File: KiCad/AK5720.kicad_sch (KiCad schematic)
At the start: 20 parts, among them J6 AudioJack3_Dual_Switch, U4 AK5720VT

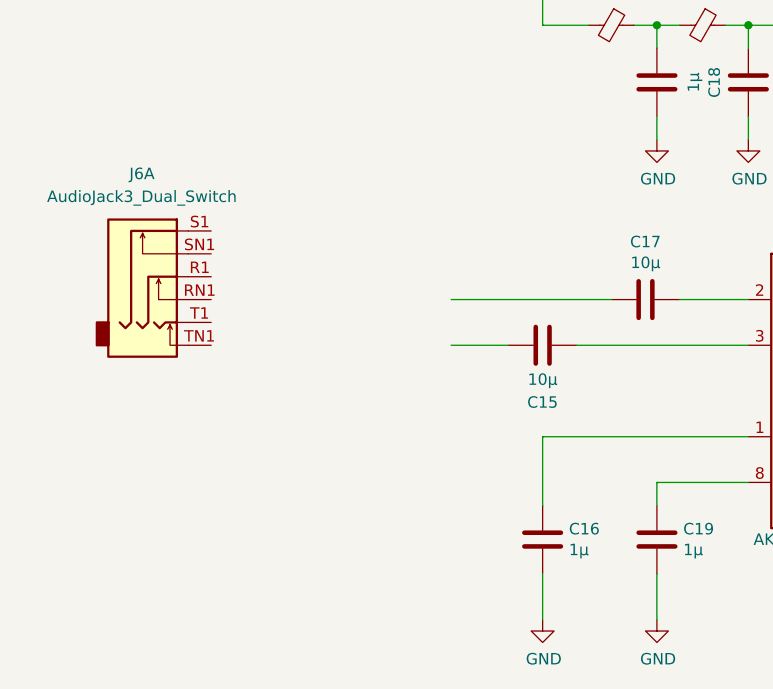
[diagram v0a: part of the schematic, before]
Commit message: -associated footprints to more specific components -added manufacturer and part series info to more specific components
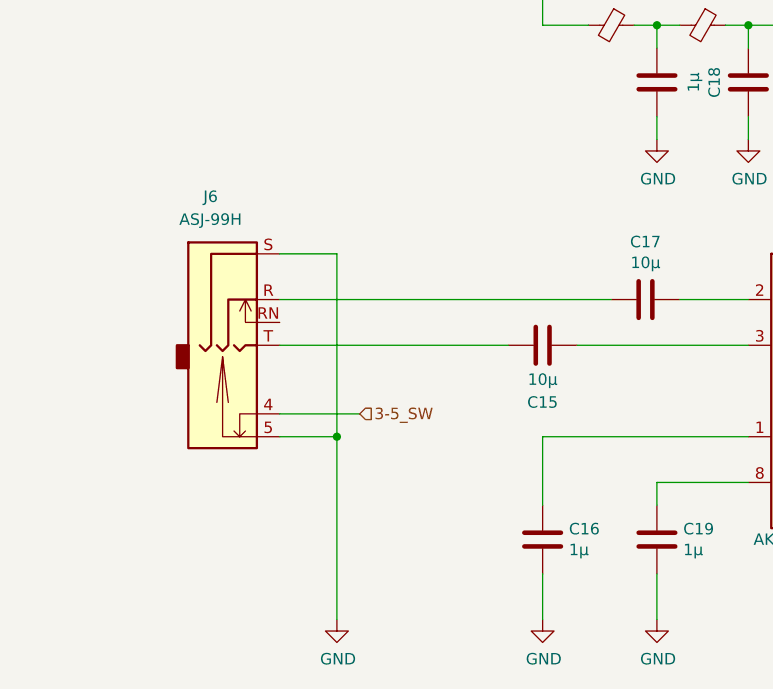
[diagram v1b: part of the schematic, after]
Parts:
- J6: value AudioJack3_Dual_Switch -> ASJ-99H; footprint (none) -> custom_footprints:ASJ-99H; symbol Connector:AudioJack3_Dual_Switch -> custom_symbols:AudioJack_ASJ-99H; MFG (none) -> Adam Tech; MFG# (none) -> ASJ-99H-R-HT-T/R
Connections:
- net GND: now also J6.5, J6.S
- net at C15.2: now also J6.T
- net at C17.2: now also J6.R
- new net 3-5_SW: J6.4
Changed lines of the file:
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@@
   (junction (at 142.24 68.58) (diameter 0) (color 0 0 0 0)
   )
+  (junction (at 81.28 114.3) (diameter 0) (color 0 0 0 0)
+  )
   (junction (at 198.12 114.3) (diameter 0) (color 0 0 0 0)
   )
@@
     (stroke (width 0) (type default) (color 0 0 0 0))
   )
-  (wire (pts (xy 100.33 104.14) (xy 93.98 104.14))
+  (wire (pts (xy 74.93 104.14) (xy 100.33 104.14))
     (stroke (width 0) (type default) (color 0 0 0 0))
   )
@@
     (stroke (width 0) (type default) (color 0 0 0 0))
   )
+  (wire (pts (xy 81.28 93.98) (xy 81.28 114.3))
+    (stroke (width 0) (type default) (color 0 0 0 0))
+  )
   (wire (pts (xy 190.5 134.62) (xy 190.5 132.08))
     (stroke (width 0) (type default) (color 0 0 0 0))
@@
     (stroke (width 0) (type default) (color 0 0 0 0))
   )
+  (wire (pts (xy 74.93 111.76) (xy 83.82 111.76))
+    (stroke (width 0) (type default) (color 0 0 0 0))
+  )
   (wire (pts (xy 152.4 121.92) (xy 182.88 121.92))
     (stroke (width 0) (type default) (color 0 0 0 0))
@@
     (stroke (width 0) (type default) (color 0 0 0 0))
   )
+  (wire (pts (xy 81.28 114.3) (xy 81.28 134.62))
+    (stroke (width 0) (type default) (color 0 0 0 0))
+  )
+  (wire (pts (xy 74.93 114.3) (xy 81.28 114.3))
+    (stroke (width 0) (type default) (color 0 0 0 0))
+  )
   (wire (pts (xy 114.3 68.58) (xy 116.84 68.58))
     (stroke (width 0) (type default) (color 0 0 0 0))
@@
     (stroke (width 0) (type default) (color 0 0 0 0))
   )
-  (wire (pts (xy 111.76 99.06) (xy 93.98 99.06))
+  (wire (pts (xy 74.93 99.06) (xy 111.76 99.06))
     (stroke (width 0) (type default) (color 0 0 0 0))
   )
@@
     (stroke (width 0) (type default) (color 0 0 0 0))
   )
+  (wire (pts (xy 74.93 93.98) (xy 81.28 93.98))
+    (stroke (width 0) (type default) (color 0 0 0 0))
+  )
   (wire (pts (xy 116.84 81.28) (xy 116.84 78.74))
     (stroke (width 0) (type default) (color 0 0 0 0))
@@
   )
   (hierarchical_label "SDWS" (shape output) (at 165.1 101.6 0)
+    (effects (font (size 1.27 1.27)) (justify left))
+  )
+  (hierarchical_label "3-5_SW" (shape input) (at 83.82 111.76 0)
     (effects (font (size 1.27 1.27)) (justify left))
   )
@@
     (pin "2")
   )
-  (symbol (lib_id "Connector:AudioJack3_Dual_Switch") (at 62.23 96.52 0) (unit 1)
+  (symbol (lib_id "custom_symbols:AudioJack_ASJ-99H") (at 69.85 99.06 0) (unit 1)
     (in_bom yes) (on_board yes) (fields_autoplaced)
-    (property "Reference" "J6" (id 0) (at 59.6265 85.09 0))
-    (property "Value" "AudioJack3_Dual_Switch" (id 1) (at 59.6265 87.63 0))
-    (property "Footprint" "" (id 2) (at 60.96 96.52 0)
-      (effects (font (size 1.27 1.27)) hide)
-    )
-    (property "Datasheet" "~" (id 3) (at 60.96 96.52 0)
-      (effects (font (size 1.27 1.27)) hide)
-    )
-    (pin "R1")
-    (pin "RN1")
-    (pin "S1")
-    (pin "SN1")
-    (pin "T1")
-    (pin "TN1")
-    (pin "R2")
-    (pin "RN2")
-    (pin "S2")
-    (pin "SN2")
-    (pin "T2")
-    (pin "TN2")
+    (property "Reference" "J6" (id 0) (at 67.2465 87.63 0))
+    (property "Value" "ASJ-99H" (id 1) (at 67.2465 90.17 0))
+    (property "Footprint" "custom_footprints:ASJ-99H" (id 2) (at 69.85 99.06 0)
+      (effects (font (size 1.27 1.27)) hide)
+    )
+    (property "Datasheet" "~" (id 3) (at 69.85 99.06 0)
+      (effects (font (size 1.27 1.27)) hide)
+    )
+    (property "MFG" "Adam Tech" (id 4) (at 69.85 99.06 0)
+      (effects (font (size 1.27 1.27)) hide)
+    )
+    (property "MFG#" "ASJ-99H-R-HT-T/R" (id 5) (at 69.85 99.06 0)
+      (effects (font (size 1.27 1.27)) hide)
+    )
+    (pin "4")
+    (pin "5")
+    (pin "R")
+    (pin "RN")
+    (pin "S")
+    (pin "T")
+  )
+  (symbol (lib_id "power:GND") (at 81.28 134.62 0) (unit 1)
+    (in_bom yes) (on_board yes)
+    (property "Reference" "#PWR?" (id 0) (at 81.28 140.97 0)
+      (effects (font (size 1.27 1.27)) hide)
+    )
+    (property "Value" "GND" (id 1) (at 81.407 139.0142 0))
+    (property "Footprint" "" (id 2) (at 81.28 134.62 0)
+      (effects (font (size 1.27 1.27)) hide)
+    )
+    (property "Datasheet" "" (id 3) (at 81.28 134.62 0)
+      (effects (font (size 1.27 1.27)) hide)
+    )
+    (pin "1")
   )
   (symbol (lib_id "power:+3V3") (at 142.24 64.77 0) (unit 1)

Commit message: -boards on hand atm, assembling first board and finalizing used component values
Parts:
- C15, C17: value 10µ -> 1u
- C16, C18, C19, C21: value 1µ -> 1u
- C20: value 220n -> 1u
- R32: value R -> 22R
- R33, R35, R38, R40: value R -> 0R
- R34, R36, R37, R39: value R -> NP
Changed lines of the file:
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@@
       (effects (font (size 1.27 1.27)) (justify left))
     )
-    (property "Value" "R" (id 1) (at 207.518 129.413 0)
+    (property "Value" "0R" (id 1) (at 207.518 129.413 0)
       (effects (font (size 1.27 1.27)) (justify left))
     )
@@
     (in_bom yes) (on_board yes)
     (property "Reference" "C15" (id 0) (at 104.14 110.49 90))
-    (property "Value" "10µ" (id 1) (at 104.14 107.95 90))
+    (property "Value" "1u" (id 1) (at 104.14 107.95 90))
     (property "Footprint" "Capacitor_SMD:C_0603_1608Metric" (id 2) (at 100.33 105.1052 0)
       (effects (font (size 1.27 1.27)) hide)
@@
       (effects (font (size 1.27 1.27)) (justify left))
     )
-    (property "Value" "R" (id 1) (at 199.898 129.413 0)
+    (property "Value" "0R" (id 1) (at 199.898 129.413 0)
       (effects (font (size 1.27 1.27)) (justify left))
     )
@@
       (effects (font (size 1.27 1.27)) (justify left))
     )
-    (property "Value" "R" (id 1) (at 199.898 104.013 0)
+    (property "Value" "NP" (id 1) (at 199.898 104.013 0)
       (effects (font (size 1.27 1.27)) (justify left))
     )
@@
     (in_bom yes) (on_board yes)
     (property "Reference" "C18" (id 0) (at 123.2408 74.93 90))
-    (property "Value" "1µ" (id 1) (at 120.9294 74.93 90))
+    (property "Value" "1u" (id 1) (at 120.9294 74.93 90))
     (property "Footprint" "Capacitor_SMD:C_0603_1608Metric" (id 2) (at 115.8748 71.12 0)
       (effects (font (size 1.27 1.27)) hide)
@@
       (effects (font (size 1.27 1.27)) (justify left))
     )
-    (property "Value" "R" (id 1) (at 159.893 94.742 0)
+    (property "Value" "22R" (id 1) (at 159.893 94.742 0)
       (effects (font (size 1.27 1.27)) (justify left))
     )
@@
       (effects (font (size 1.27 1.27)) (justify left))
     )
-    (property "Value" "1µ" (id 1) (at 119.761 126.873 0)
+    (property "Value" "1u" (id 1) (at 119.761 126.873 0)
       (effects (font (size 1.27 1.27)) (justify left))
     )
@@
     (in_bom yes) (on_board yes)
     (property "Reference" "C21" (id 0) (at 153.7208 74.93 90))
-    (property "Value" "1µ" (id 1) (at 151.4094 74.93 90))
+    (property "Value" "1u" (id 1) (at 151.4094 74.93 90))
     (property "Footprint" "Capacitor_SMD:C_0603_1608Metric" (id 2) (at 146.3548 71.12 0)
       (effects (font (size 1.27 1.27)) hide)
@@
       (effects (font (size 1.27 1.27)) (justify left))
     )
-    (property "Value" "R" (id 1) (at 207.518 104.013 0)
+    (property "Value" "NP" (id 1) (at 207.518 104.013 0)
       (effects (font (size 1.27 1.27)) (justify left))
     )
@@
       (effects (font (size 1.27 1.27)) (justify left))
     )
-    (property "Value" "R" (id 1) (at 184.658 104.013 0)
+    (property "Value" "0R" (id 1) (at 184.658 104.013 0)
       (effects (font (size 1.27 1.27)) (justify left))
     )
@@
       (effects (font (size 1.27 1.27)) (justify left))
     )
-    (property "Value" "R" (id 1) (at 192.278 129.413 0)
+    (property "Value" "NP" (id 1) (at 192.278 129.413 0)
       (effects (font (size 1.27 1.27)) (justify left))
     )
@@
       (effects (font (size 1.27 1.27)) (justify left))
     )
-    (property "Value" "R" (id 1) (at 192.278 104.013 0)
+    (property "Value" "0R" (id 1) (at 192.278 104.013 0)
       (effects (font (size 1.27 1.27)) (justify left))
     )
@@
       (effects (font (size 1.27 1.27)) (justify left))
     )
-    (property "Value" "1µ" (id 1) (at 107.061 126.873 0)
+    (property "Value" "1u" (id 1) (at 107.061 126.873 0)
       (effects (font (size 1.27 1.27)) (justify left))
     )
@@
     (in_bom yes) (on_board yes)
     (property "Reference" "C17" (id 0) (at 115.57 92.6592 90))
-    (property "Value" "10µ" (id 1) (at 115.57 94.9706 90))
+    (property "Value" "1u" (id 1) (at 115.57 94.9706 90))
     (property "Footprint" "Capacitor_SMD:C_0603_1608Metric" (id 2) (at 111.76 100.0252 0)
       (effects (font (size 1.27 1.27)) hide)
@@
       (effects (font (size 1.27 1.27)) (justify left))
     )
-    (property "Value" "R" (id 1) (at 184.658 129.413 0)
+    (property "Value" "NP" (id 1) (at 184.658 129.413 0)
       (effects (font (size 1.27 1.27)) (justify left))
     )
@@
     (in_bom yes) (on_board yes)
     (property "Reference" "C20" (id 0) (at 133.4008 74.93 90))
-    (property "Value" "220n" (id 1) (at 131.0894 74.93 90))
+    (property "Value" "1u" (id 1) (at 131.0894 74.93 90))
     (property "Footprint" "Capacitor_SMD:C_0603_1608Metric" (id 2) (at 126.0348 71.12 0)
       (effects (font (size 1.27 1.27)) hide)
